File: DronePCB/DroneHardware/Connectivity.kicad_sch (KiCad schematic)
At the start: 10 parts, among them J201 USB_B_Mini, J202 BATTERY, J203 I2C_CONN, J204 SWD_CONN, J205 USART6_CONN, U201 USBLC6-2SC6

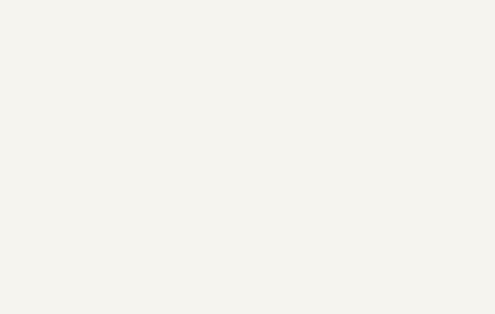
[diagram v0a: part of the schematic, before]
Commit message: Inizio collegamenti MPU-6000
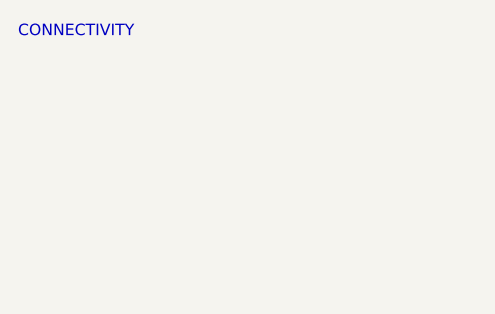
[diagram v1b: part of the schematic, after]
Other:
- note added: "CONNECTIVITY"
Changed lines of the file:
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@@
+    (effects (font (size 1.27 1.27)) (justify left bottom))
+  )
+  (text "CONNECTIVITY\n" (at 13.462 14.986 0)
     (effects (font (size 1.27 1.27)) (justify left bottom))
   )

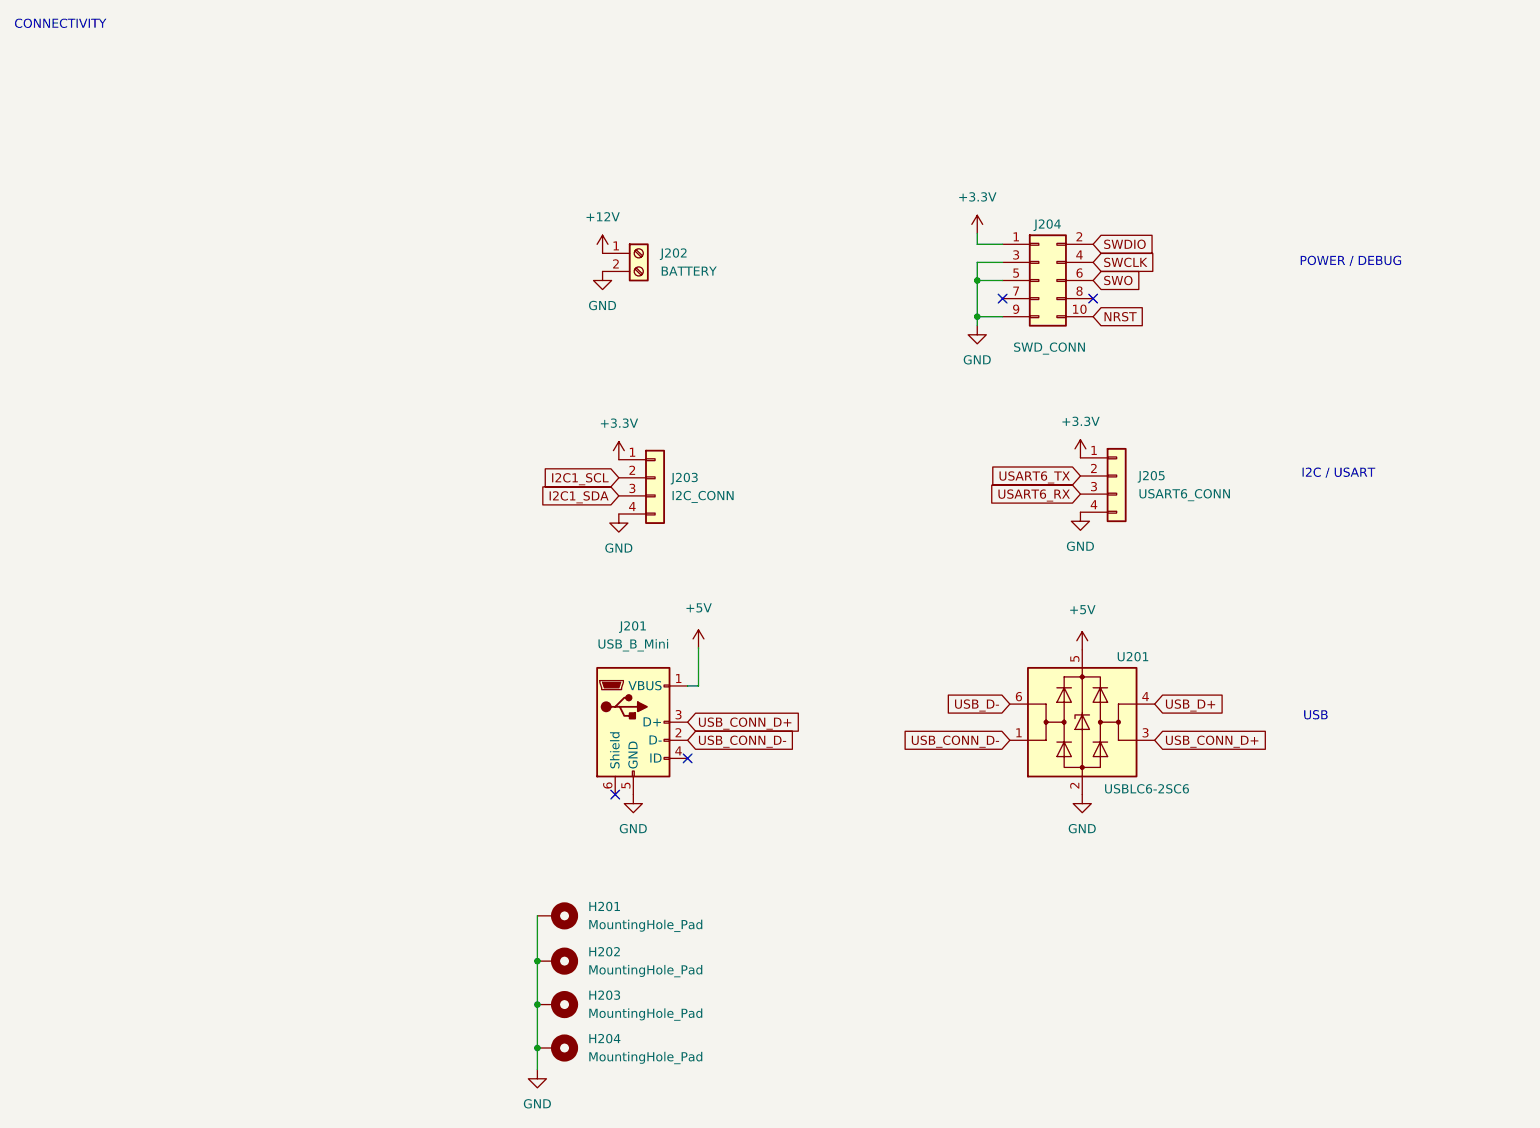
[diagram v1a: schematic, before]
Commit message: Creazione PCB e utilizzo di processore STM32F405
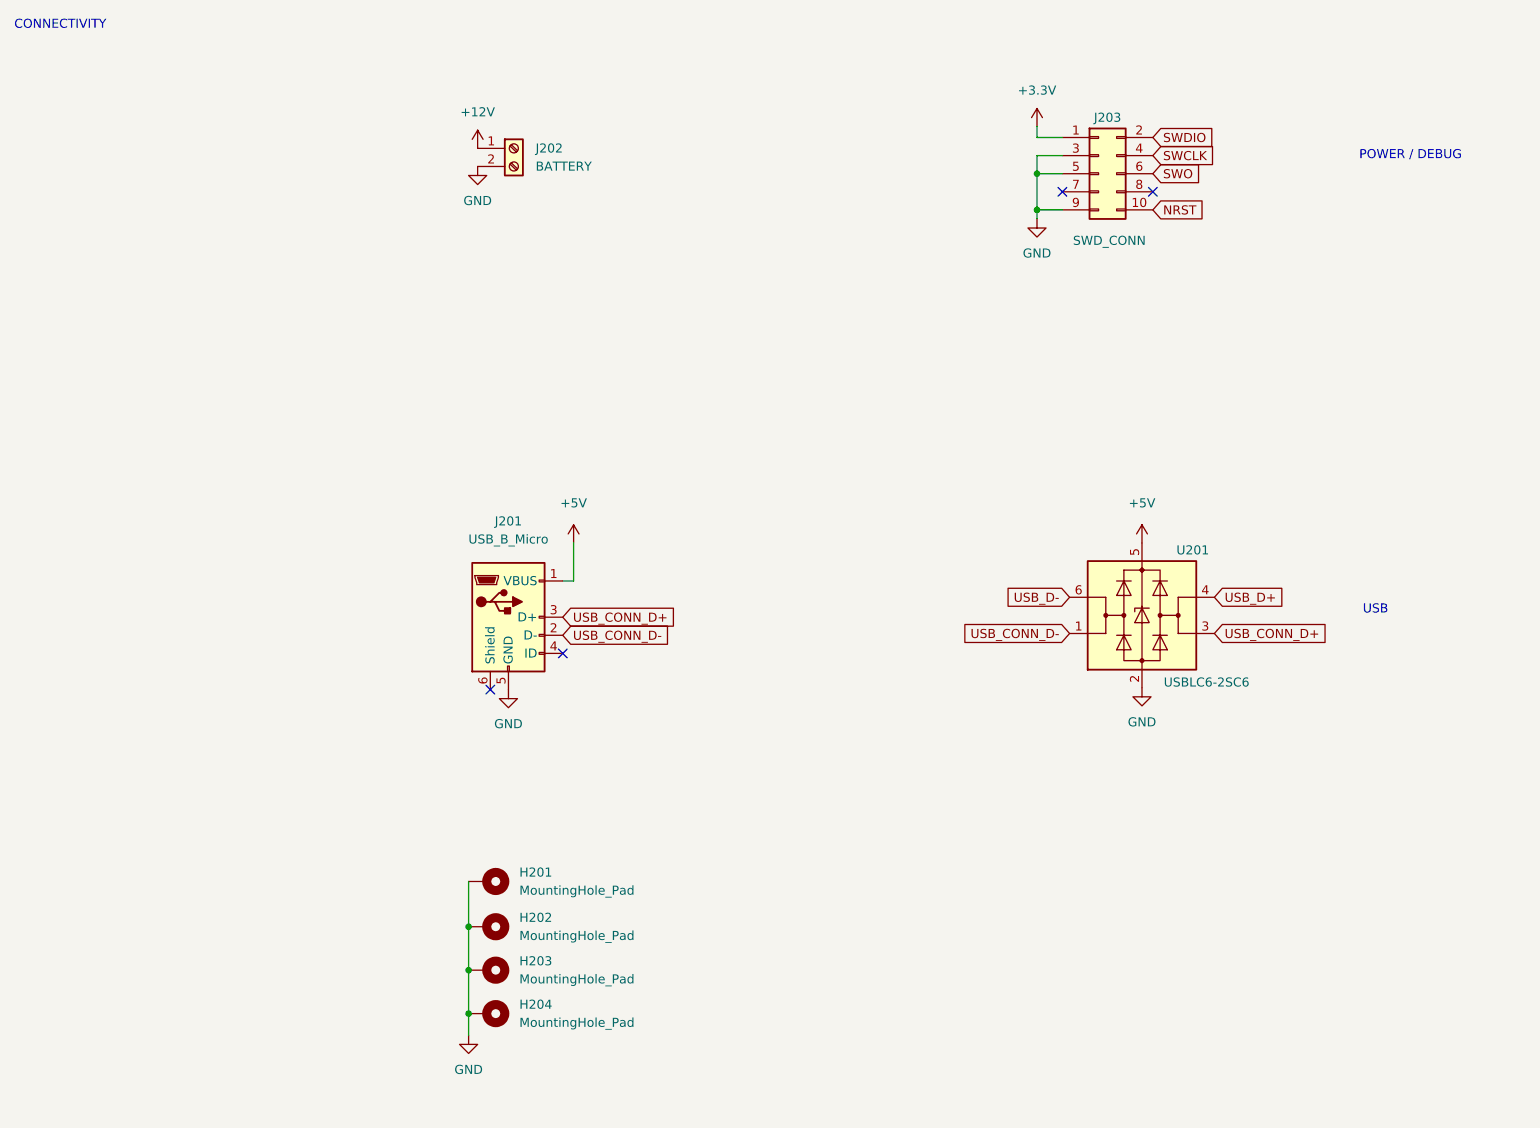
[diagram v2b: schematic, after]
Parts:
- removed J201: USB_B_Mini, Connector_USB:USB_Mini-B_Wuerth_65100516121_Horizontal, symbol Connector:USB_B_Mini
- removed J203: I2C_CONN, Connector_Molex:Molex_PicoBlade_53048-0410_1x04_P1.25mm_Horizontal, symbol Connector_Generic:Conn_01x04
- removed J205: USART6_CONN, Connector_Molex:Molex_PicoBlade_53048-0410_1x04_P1.25mm_Horizontal, symbol Connector_Generic:Conn_01x04
- added J201: USB_B_Micro, Connector_USB:USB_Micro-AB_Molex_47590-0001, symbol Connector:USB_B_Micro
- H201, H202, H203, H204: footprint MountingHole:MountingHole_4.3mm_M4_Pad_Via -> MountingHole:MountingHole_3.2mm_M3
- J202: footprint TerminalBlock_Phoenix:TerminalBlock_Phoenix_PT-1,5-2-3.5-H_1x02_P3.50mm_Horizontal -> Connector_PinHeader_1.00mm:PinHeader_1x02_P1.00mm_Vertical
- renumbered J204 to J203
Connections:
- net +5V: now also J201.1 (VBUS)
- net GND: now also J201.5 (GND)
- net USB_CONN_D+: now also J201.3 (D+)
- net USB_CONN_D-: now also J201.2 (D-)
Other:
- note removed: "I2C / USART"
- moved on the sheet: H201, H202, H203, H204, J202, J203, U201

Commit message: Modifica della porta USB
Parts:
- J201: footprint Connector_USB:USB_Micro-AB_Molex_47590-0001 -> Connector_USB:USB_Micro-B_Molex-105017-0001
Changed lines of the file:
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@@
     (property "Reference" "J201" (id 0) (at 82.804 83.82 0))
     (property "Value" "USB_B_Micro" (id 1) (at 82.804 86.36 0))
-    (property "Footprint" "Connector_USB:USB_Micro-AB_Molex_47590-0001" (id 2) (at 86.614 98.552 0)
+    (property "Footprint" "Connector_USB:USB_Micro-B_Molex-105017-0001" (id 2) (at 86.614 98.552 0)
       (effects (font (size 1.27 1.27)) hide)
     )

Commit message: Aggiornamento delle tracce
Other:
- moved on the sheet: J202, J203
